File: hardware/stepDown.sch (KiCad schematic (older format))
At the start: 18 parts

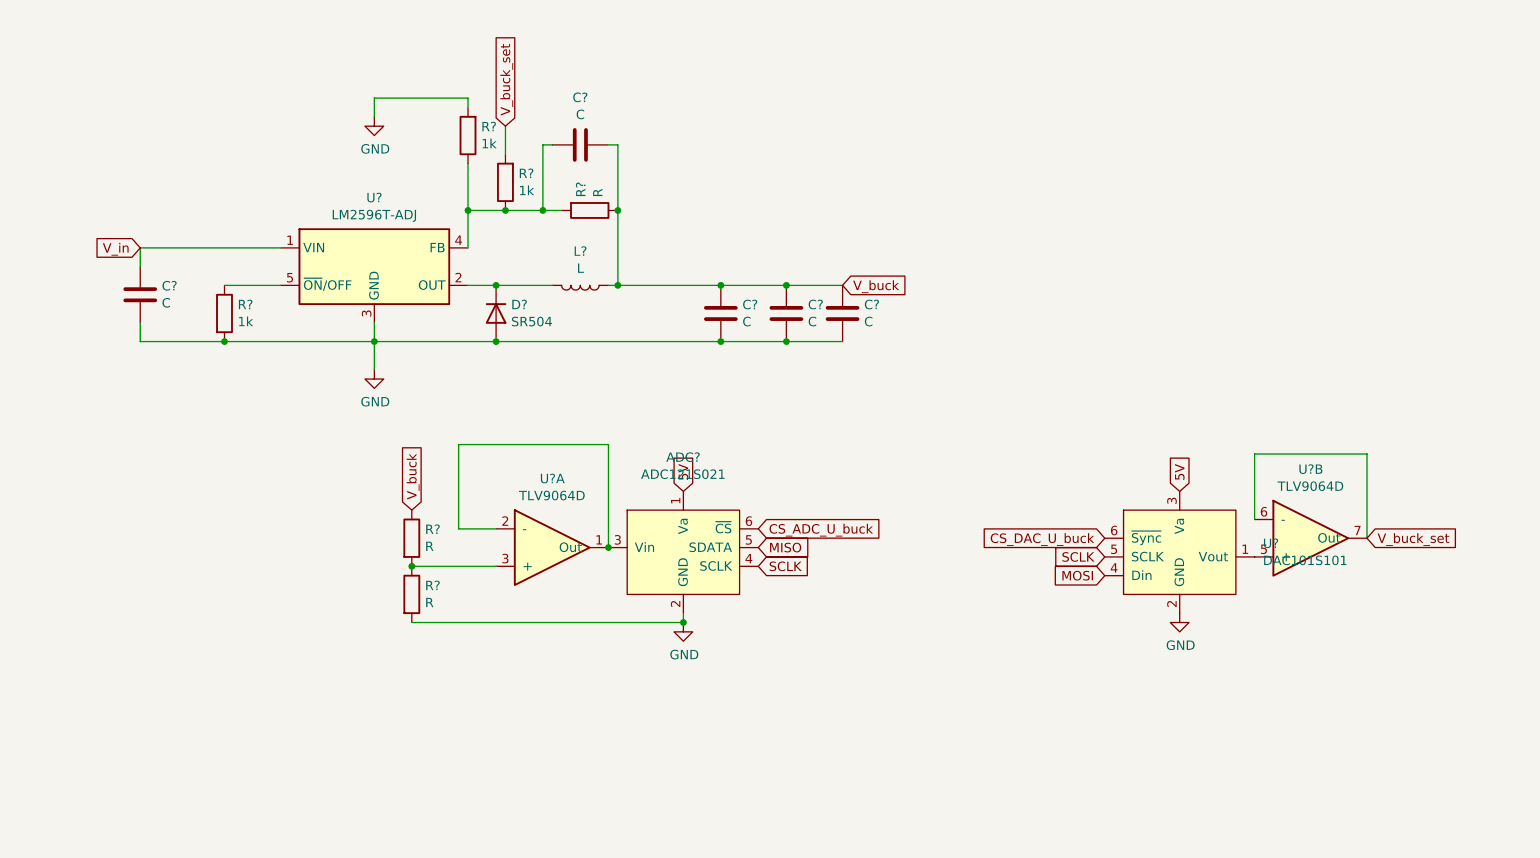
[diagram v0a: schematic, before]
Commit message: switched to xl4016 and worked on control board
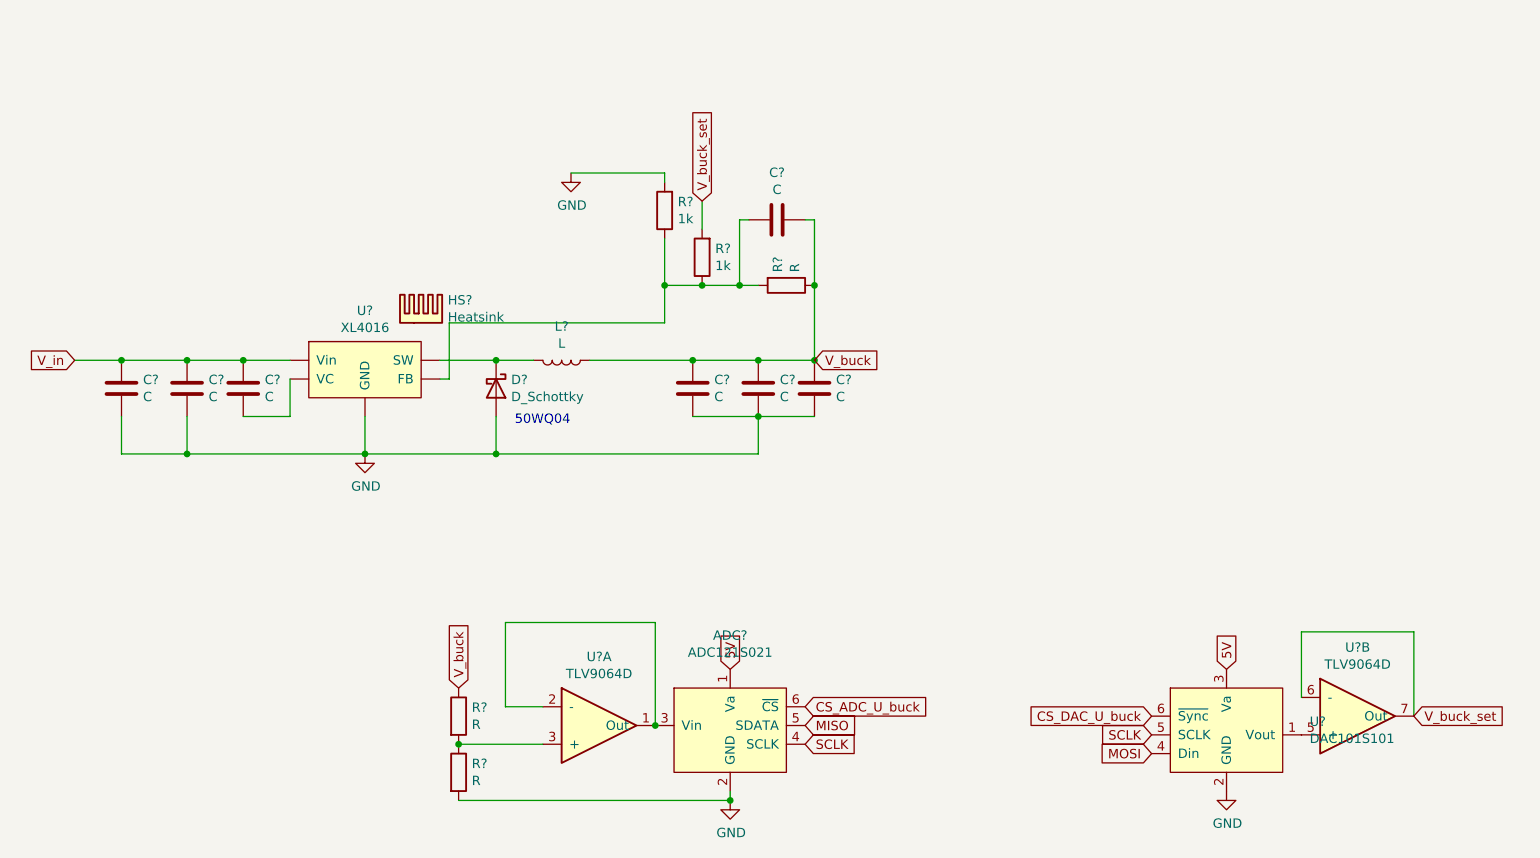
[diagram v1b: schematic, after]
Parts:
- removed C? (x5): C, symbol Device:C
- removed D?: SR504, symbol Device:D
- removed L?: L, symbol Device:L
- removed R?: R, symbol Device:R
- removed R? (x3): 1k, symbol Device:R
- removed U?: LM2596T-ADJ, Package_TO_SOT_THT:TO-220-5_P3.4x3.7mm_StaggerOdd_Lead3.8mm_Vertical, symbol Regulator_Switching:LM2596T-ADJ
- added C? (x7): C, symbol Device:C
- added D?: D_Schottky, symbol Device:D_Schottky
- added HS?: Heatsink, symbol Mechanical:Heatsink
- added L?: L, symbol Device:L
- added R?: R, symbol Device:R
- added R? (x2): 1k, symbol Device:R
- added U?: XL4016, symbol Custom:XL4016
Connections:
- net GND: now also C?.2, C?.2, C?.2, C?.2, C?.2, D?.2 (A), R?.2, U?.~ (Vin)
- net V_buck: now also C?.1, C?.1, C?.1, C?.1, L?.1, R?.1
- net V_buck_set: now also R?.2
- net V_in: now also C?.1, C?.1, C?.1, U?.~ (Vin)
- new net: C?.2, U?.~ (Vin)
- new net: D?.1 (K), L?.2, U?.~ (Vin)
- new net: C?.2, R?.1, R?.1, R?.2, U?.~ (Vin)
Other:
- note added: "50WQ04"
- moved on the sheet: ADC?, R?, U?, U?A, U?B
